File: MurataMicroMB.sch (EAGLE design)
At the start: 63 parts, among them CON1 CON_MICROSD_C2395, CON2 WM17143CT-ND, CON3 CON_MIL_10_ARM, CON4 CON_MICROSD_C2395, IC1 NC7SZ00M5XCT-ND, IC2 296-35164-1-ND, IC3 IC_LPC11U3XQFN33, IC4 LDO4_3.3_SOT223, Q1 1253-1168-1-ND, SW1 P-8073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

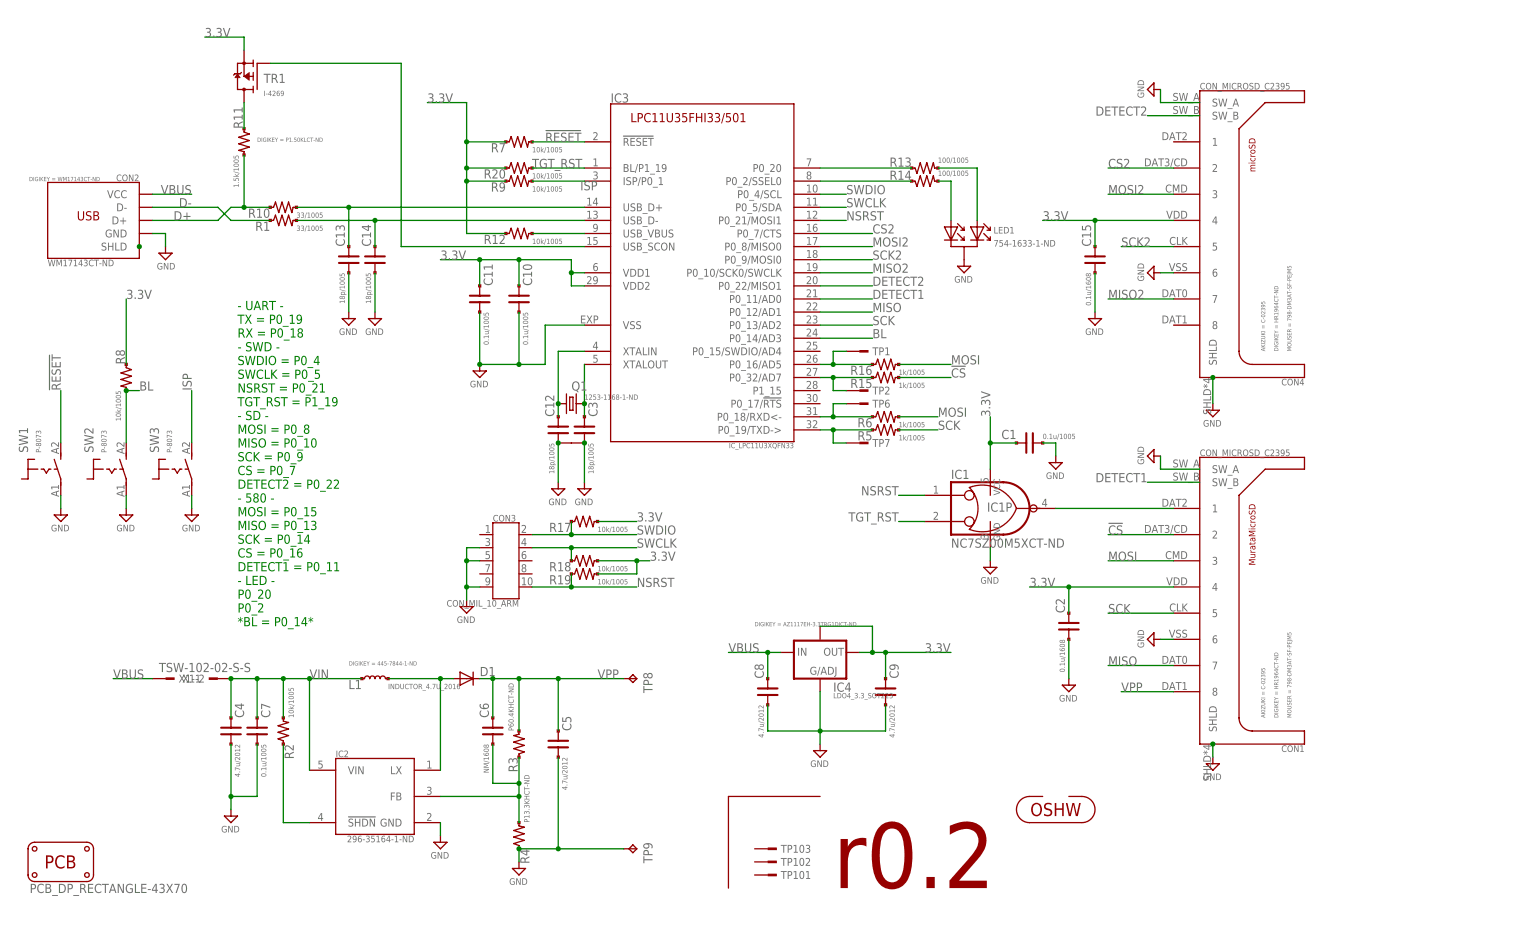
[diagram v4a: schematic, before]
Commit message: [ MB ] update package of LED1; add TP_4020; update package of IC2
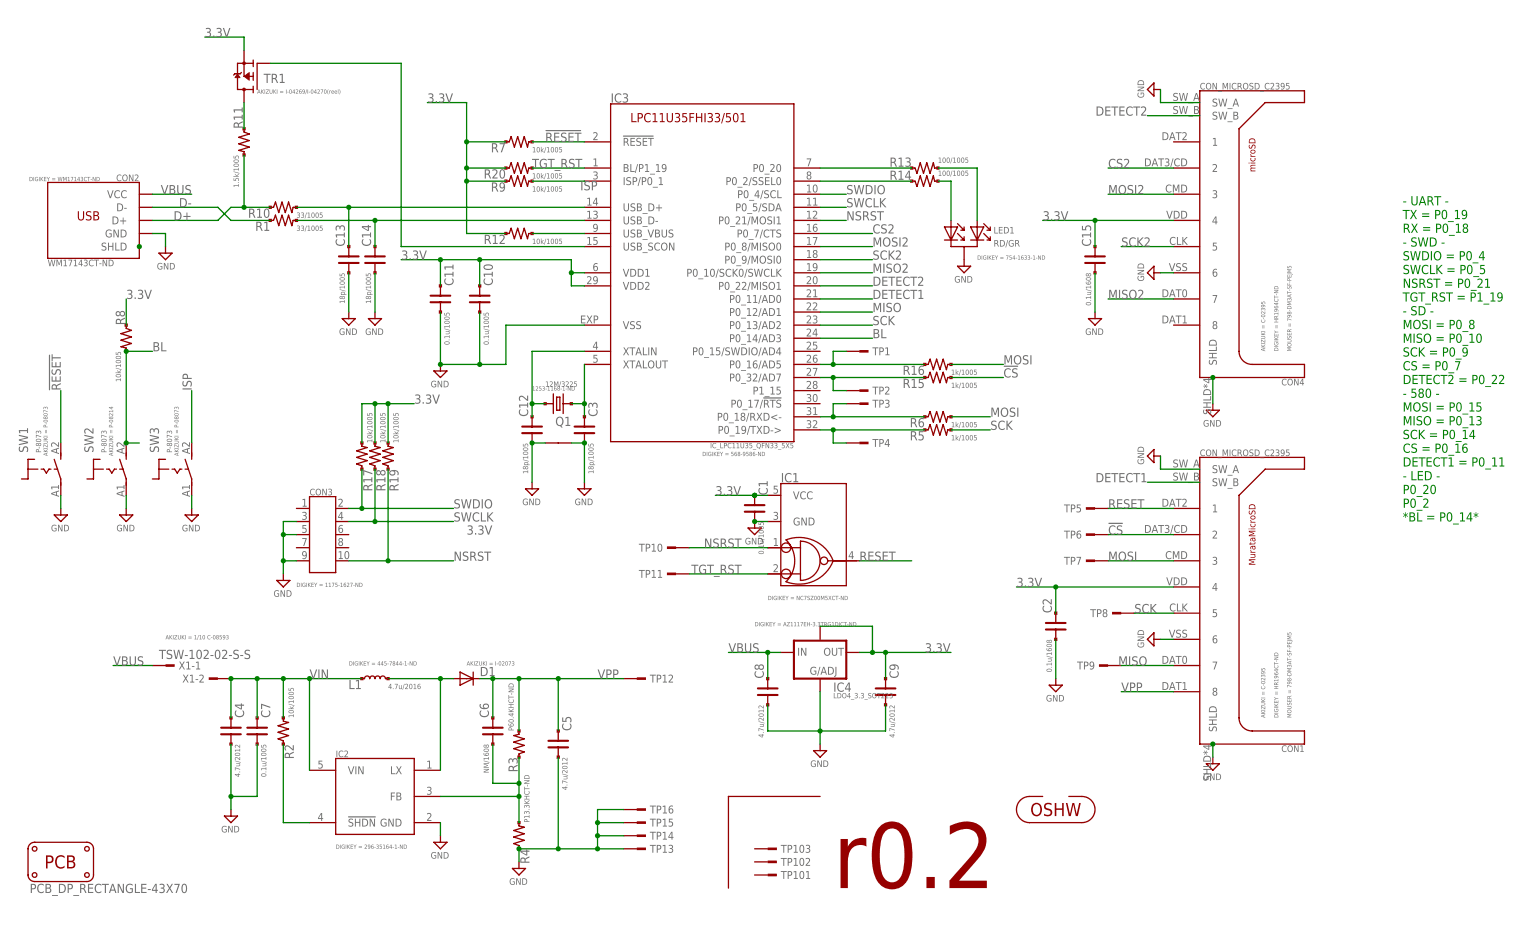
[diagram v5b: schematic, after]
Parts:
- added TP10, TP11, TP12, TP5: (no value), mylib:TESTPAD
- added TP13, TP14, TP15, TP16: (no value), mylib:TESTPAD_4020
- added TP3, TP4: TESTPAD_1608, mylib:TESTPAD_1608
- CON3: value CON_MIL_10_ARM -> (none)
- D1: value DIODE_SMALL -> 40V2A; device mylib:DIODE_SMALL -> mylib:DIODE2_40V2A_SOD123
- IC1: value NC7SZ00M5XCT-ND -> (none); device 74xx-little-us_local:74LVC1G00DBV -> mylib:IC_TTL_SINGLE_74_00_SOT23
- IC2: value 296-35164-1-ND -> (none); device mylib:IC_DCDC_LM27313 -> mylib:IC_DCDC_LM27313_SOT23
- IC3: value IC_LPC11U3XQFN33 -> IC_LPC11U35_QFN33_5X5; device mylib:IC_LPC11U3XQFN33 -> mylib:IC_LPC11U35_QFN33_5X5
- L1: value INDUCTOR_4.7U_2016 -> 4.7u/2016
- LED1: value 754-1633-1-ND -> RD/GR; device mylib:LED_1SEG_A2K1 -> mylib:LED2_A2K1_GR/RD
- Q1: value 1253-1168-1-ND -> 12M/3225
- TP101, TP102, TP103: value TESTPAD_F -> (none)
- TP6, TP7: value TESTPAD_1608 -> (none); device mylib:TESTPAD_1608 -> mylib:TESTPAD
- TP8, TP9: value TPPAD1-13 -> (none); device testpad_local:TPPAD1-13 -> mylib:TESTPAD
- TR1: value I-4269 -> PMOS_BSS84_SOT23; device mylib:TR_PMOS_GDS_SOT23 -> mylib:PMOS_BSS84_SOT23
- U$1: value ICON_OSHW -> (none)
- X1: AKIZUKI (none) -> 1/10 C-08593
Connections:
- removed net N$3: CON1.1, IC1A.O
- new net RESET: CON1.1, IC1.1Y, TP5.1
- net !CS!: now also TP6.1
- net 3.3V: now also IC1.VCC; no longer IC1P.VCC
- net GND: now also IC1.GND, TP13.1, TP14.1, TP15.1, TP16.1; no longer IC1P.GND, TP9.TP
- net MISO: now also TP9.1
- net MOSI: now also TP7.1
- net N$6: now also TP3.1; no longer TP6.1
- net N$9: now also TP4.1; no longer TP7.1
- net NSRST: now also IC1.1A, TP10.1; no longer IC1A.I0
- net SCK: now also TP8.1
- net TGT_RST: now also IC1.1B, TP11.1; no longer IC1A.I1
- net VPP: now also TP12.1; no longer TP8.TP
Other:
- moved on the sheet: C1, C10, C11, C12, C2, CON3, Q1, R15, R16, R17, R18, R19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

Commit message: [ MB ] TP12;IC4;CON2
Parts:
- IC4: value LDO4_3.3_SOT223 -> (none)
